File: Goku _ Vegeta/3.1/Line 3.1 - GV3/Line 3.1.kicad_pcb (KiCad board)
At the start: 2 copper layers, 112 parts, among them J1 Solenoid, J10 RIGHT HEADERS, J11 Kicker Voltmeter, J3 Motor 1, J4 Motor 3, J5 Motor 2, J6 Motor 4, J7 BATTERY POWER, J8 I2C TO MASTER, J9 LEFT HEADERS, Q2 BSC040N10NS5, U1 LM2587S-ADJ, U10 TPS62132, U11 TPS62133, U2 TB67H420FTG Dual/Single Motor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, U3 TB67H420FTG Dual/Single Motor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, U4 TB67H420FTG Dual/Single Motor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, U5 TB67H420FTG Dual/Single Motor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, U7 NXV55UNR, U9 DEV-16771

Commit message: move to 3.1
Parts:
- removed C1, C6: 100uF, Capacitor_THT:CP_Radial_D10.0mm_P5.00mm
- removed C10, C16: 0.1uF, Capacitor_SMD:C_0805_2012Metric
- removed C15, C8: 10uF, Capacitor_SMD:C_0805_2012Metric
- removed C17, C9: 3.3nF, Capacitor_SMD:C_0805_2012Metric
- removed C18, C7: 22uF, Capacitor_SMD:C_0805_2012Metric
- removed C2, C5: 1uF, Capacitor_SMD:C_0805_2012Metric
- removed C3, C4: 560uF, Capacitor_THT:CP_Radial_D18.0mm_P7.50mm
- removed D1: SS510, Diode_SMD:D_SOD-128
- removed D2, D3, D5: STTH2002G-TR, Package_TO_SOT_SMD:TO-263-2
- removed J1: Solenoid, TerminalBlock:TerminalBlock_bornier-2_P5.08mm
- removed J10: RIGHT HEADERS, Connector_PinHeader_2.54mm:PinHeader_1x24_P2.54mm_Vertical
- removed J3: Motor 1, Connector_PinSocket_2.54mm:PinSocket_1x06_P2.54mm_Vertical
- removed J5: Motor 2, Connector_PinSocket_2.54mm:PinSocket_1x06_P2.54mm_Vertical
- removed J6: Motor 4, Connector_PinSocket_2.54mm:PinSocket_1x06_P2.54mm_Vertical
- removed J7: BATTERY POWER, Connector_AMASS:AMASS_XT60-F_1x02_P7.20mm_Vertical
- removed J8: I2C TO MASTER, Connector_JST:JST_XH_B4B-XH-AM_1x04_P2.50mm_Vertical
- removed J9: LEFT HEADERS, Connector_PinHeader_2.54mm:PinHeader_1x24_P2.54mm_Vertical
- removed L1: 56uH, Inductor_SMD:L_Bourns_SRR1260
- removed L2, L3: 2.2uH, Inductor_SMD:L_Bourns_SRR1260
- removed Q2: BSC040N10NS5, Package_TO_SOT_SMD:TDSON-8-1
- removed R33, R35, R37, R39: 10K, Resistor_SMD:R_0805_2012Metric
- removed R34, R36, R38: 12R, Resistor_SMD:R_0805_2012Metric
- removed U1: LM2587S-ADJ, LM2587S-ADJ:VREG_TPS79625KTTR
- removed U10: TPS62132, Package_DFN_QFN:VQFN-16-1EP_3x3mm_P0.5mm_EP1.68x1.68mm_ThermalVias
- removed U11: TPS62133, Package_DFN_QFN:VQFN-16-1EP_3x3mm_P0.5mm_EP1.68x1.68mm_ThermalVias
- removed U2, U3, U4, U5: TB67H420FTG Dual/Single Motor Driver Carrier, TB67H420FTG Dual_Single Motor Driver Carrier:TB67H420FTG DualSingle Motor Driver Carrier
- removed U7: NXV55UNR, NXV55UNR:TRANS_BC846B,215
- removed U9: DEV-16771, DEV-16771:MODULE_DEV-16771
- added J12: RIGHT HEADERS, Connector_PinHeader_2.54mm:PinHeader_1x24_P2.54mm_Vertical, F.Cu at (139.0, 247.2)
- added J13: MID HEADERS, Connector_PinHeader_2.54mm:PinHeader_1x05_P2.54mm_Vertical, F.Cu at (144.9, 183.5)
- added J2: BACKUP 5V, Connector_AMASS:AMASS_XT30U-F_1x02_P5.0mm_Vertical, F.Cu at (78.8, 124.5)
- added U8: DEV-16771, DEV-16771:MODULE_DEV-16771, F.Cu at (150.0, 218.0)
- A1, A10, A11, A12, A13, A14, A15, A16, A2, A3, A4, A5, A6, A7, A8, A9, LED1, LED10, LED11, LED12, LED13, LED14, LED15, LED16, LED2, LED3, LED4, LED5, LED6, LED7, LED8, LED9, R10, R12, R14, R16, R26, R28: moved to B.Cu
- J11: value Kicker Voltmeter -> LEFT HEADERS; footprint TerminalBlock:TerminalBlock_bornier-2_P5.08mm -> Connector_PinHeader_2.54mm:PinHeader_1x24_P2.54mm_Vertical
- J4: value Motor 3 -> I2C; footprint Connector_PinSocket_2.54mm:PinSocket_1x06_P2.54mm_Vertical -> Connector_AMASS:AMASS_XT30U-F_1x02_P5.0mm_Vertical
- R1: value 2K94 -> 36R; moved to B.Cu
- R11, R13, R15, R25, R27, R31, R9: value 12R -> 10K; moved to B.Cu
- R17, R19, R21, R23, R4, R6: value 12R -> 36R; moved to B.Cu
- R18, R20, R22, R24, R5, R7, R8: value 10K -> 36R; moved to B.Cu
- R2: value 57K -> 36R; moved to B.Cu
- R29: value CT6EP103 -> 10K; footprint POT_CT-6EP_NDC:POT_CT-6EP_NDC -> Resistor_SMD:R_0805_2012Metric; moved to B.Cu
- R3: value 1K5 -> 36R; moved to B.Cu
- R30, R32: value 100K -> 10K; moved to B.Cu
- moved A2 149.1 mm to (230.0, 150.0), turned to 90 degrees
- moved R11 124.0 mm to (154.0, 227.0), turned to -90 degrees
- moved R3 123.2 mm to (146.0, 227.0), turned to 90 degrees
- moved R2 119.4 mm to (227.0, 154.0), turned to 180 degrees
- moved A6 118.9 mm to (200.0, 150.0), turned to 90 degrees
- moved R10 112.1 mm to (227.0, 146.0)
- moved A3 109.8 mm to (150.0, 230.0)
- moved LED2 109.7 mm to (227.0, 150.0), turned to -90 degrees
- moved A1 98.1 mm to (150.0, 70.0), turned to 180 degrees
- moved LED3 97.7 mm to (150.0, 227.0), turned to 180 degrees
- moved J11 95.2 mm to (161.0, 247.2), turned to 180 degrees
- moved A7 88.3 mm to (150.0, 200.0)
- moved R6 87.2 mm to (197.0, 154.0), turned to 180 degrees
- moved A5 84.7 mm to (150.0, 100.0), turned to 180 degrees
- moved A11 84.5 mm to (170.0, 150.0), turned to 90 degrees
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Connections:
- A1 pad 1: +3V3 -> +5V
- A1 pad 2: /SEN1 -> /21
- A10 pad 1: +3V3 -> +5V
- A10 pad 2: /SEN1 -> /38
- A11 pad 1: +3V3 -> +5V
- A11 pad 2: /SEN1 -> /39
- A12 pad 1: +3V3 -> +5V
- A12 pad 2: /SEN1 -> /40
- A13 pad 1: +3V3 -> +5V
- A13 pad 2: /SEN1 -> /41
- A14 pad 1: +3V3 -> +5V
- A14 pad 2: /SEN1 -> /14
- A15 pad 1: +3V3 -> +5V
- A15 pad 2: /SEN1 -> /15
- A16 pad 1: +3V3 -> +5V
- A16 pad 2: /SEN1 -> /16
- A2 pad 1: +3V3 -> +5V
- A2 pad 2: /SEN1 -> /26
- A3 pad 1: +3V3 -> +5V
- A3 pad 2: /SEN1 -> /24
- A4 pad 1: +3V3 -> +5V
- A4 pad 2: /SEN1 -> /23
- A5 pad 1: +3V3 -> +5V
- A5 pad 2: /SEN1 -> /20
- A6 pad 1: +3V3 -> +5V
- A6 pad 2: /SEN1 -> /27
- A7 pad 1: +3V3 -> +5V
- A7 pad 2: /SEN1 -> /25
- A8 pad 1: +3V3 -> +5V
- A8 pad 2: /SEN1 -> /22
- A9 pad 1: +3V3 -> +5V
- A9 pad 2: /SEN1 -> /17
- J11 pad 1: Net-(D1-K) -> GND
- J11 pad 2: GND -> /0
- J4 pad 1: Net-(J4-Pin_1) -> /19
- J4 pad 2: Net-(J4-Pin_2) -> /18
- LED1 pad 1: /MSFTDRN -> GND
- LED10 pad 1: /MSFTDRN -> GND
- LED11 pad 1: /MSFTDRN -> GND
- LED12 pad 1: /MSFTDRN -> GND
- LED13 pad 1: /MSFTDRN -> GND
- LED14 pad 1: /MSFTDRN -> GND
- LED15 pad 1: /MSFTDRN -> GND
- LED16 pad 1: /MSFTDRN -> GND
- LED2 pad 1: /MSFTDRN -> GND
- LED3 pad 1: /MSFTDRN -> GND
- LED4 pad 1: /MSFTDRN -> GND
- LED5 pad 1: /MSFTDRN -> GND
- LED6 pad 1: /MSFTDRN -> GND
- LED7 pad 1: /MSFTDRN -> GND
- LED8 pad 1: /MSFTDRN -> GND
- LED9 pad 1: /MSFTDRN -> GND
- R1 pad 1: Net-(U1-COMP) -> +5V
- R1 pad 2: Net-(C2-Pad1) -> Net-(LED1-Pad2)
- R10 pad 2: /SEN1 -> /26
- R11 pad 1: +3V3 -> GND
- R11 pad 2: Net-(LED4-Pad2) -> /24
- R12 pad 2: /SEN1 -> /23
- R13 pad 1: +3V3 -> GND
- R13 pad 2: Net-(LED5-Pad2) -> /20
- R14 pad 2: /SEN1 -> /27
- R15 pad 1: +3V3 -> GND
- R15 pad 2: Net-(LED6-Pad2) -> /25
- R16 pad 2: /SEN1 -> /22
- R17 pad 1: +3V3 -> +5V
- R17 pad 2: Net-(LED7-Pad2) -> Net-(LED9-Pad2)
- R18 pad 1: GND -> +5V
- R18 pad 2: /SEN1 -> Net-(LED10-Pad2)
- R19 pad 1: +3V3 -> +5V
- R19 pad 2: Net-(LED8-Pad2) -> Net-(LED11-Pad2)
- R2 pad 1: Net-(D1-K) -> +5V
- R2 pad 2: Net-(R2-Pad2) -> Net-(LED2-Pad2)
- R20 pad 1: GND -> +5V
- R20 pad 2: /SEN1 -> Net-(LED12-Pad2)
- R21 pad 1: +3V3 -> +5V
- R21 pad 2: Net-(LED9-Pad2) -> Net-(LED13-Pad2)
- R22 pad 1: GND -> +5V
- R22 pad 2: /SEN1 -> Net-(LED14-Pad2)
- R23 pad 1: +3V3 -> +5V
- R23 pad 2: Net-(LED10-Pad2) -> Net-(LED15-Pad2)
- R24 pad 1: GND -> +5V
- R24 pad 2: /SEN1 -> Net-(LED16-Pad2)
- R25 pad 1: +3V3 -> GND
- R25 pad 2: Net-(LED11-Pad2) -> /17
- R26 pad 2: /SEN1 -> /38
- R27 pad 1: +3V3 -> GND
- R27 pad 2: Net-(LED12-Pad2) -> /39
- R28 pad 2: /SEN1 -> /40
- R29 pad 1: Net-(U1-FB) -> GND
- R29 pad 2: Net-(U1-FB) -> /41
- R3 pad 1: Net-(U1-FB) -> +5V
- R3 pad 2: GND -> Net-(LED3-Pad2)
- R30 pad 1: Net-(U10-PG) -> GND
- R30 pad 2: +3V3 -> /14
- R31 pad 1: +3V3 -> GND
- R31 pad 2: Net-(LED13-Pad2) -> /15
- R32 pad 1: Net-(U11-PG) -> GND
- R32 pad 2: +5V -> /16
- R4 pad 1: +3V3 -> +5V
- R4 pad 2: Net-(LED1-Pad2) -> Net-(LED4-Pad2)
- R5 pad 1: GND -> +5V
- R5 pad 2: /SEN1 -> Net-(LED5-Pad2)
- R6 pad 1: +3V3 -> +5V
- R6 pad 2: Net-(LED2-Pad2) -> Net-(LED6-Pad2)
- R7 pad 1: GND -> +5V
- R7 pad 2: /2 -> Net-(LED7-Pad2)
- R8 pad 1: GND -> +5V
- R8 pad 2: /SEN1 -> Net-(LED8-Pad2)
- R9 pad 1: +3V3 -> GND
- R9 pad 2: Net-(LED3-Pad2) -> /21
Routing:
- net +5V: track 0.00 -> 664.1 mm, vias 0 -> 13
- net /21: track 0.00 -> 186.8 mm
- net /20: track 0.00 -> 152.0 mm
- net /23: track 0.00 -> 121.8 mm
- net /17: track 0.00 -> 118.8 mm
- net /26: track 0.00 -> 110.6 mm
- net /22: track 0.00 -> 107.1 mm
- net /19: track 0.00 -> 99.7 mm, vias 0 -> 1
- net /16: track 0.00 -> 98.2 mm
- net /38: track 0.00 -> 97.8 mm
- net /18: track 0.00 -> 92.8 mm, vias 0 -> 1
- net /39: track 0.00 -> 83.0 mm
- net /27: track 0.00 -> 81.2 mm, vias 0 -> 2
- net /15: track 0.00 -> 80.5 mm
- net /14: track 0.00 -> 68.7 mm
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- added copper zone on B.Cu, net GND
- added copper zone on F.Cu, net GND
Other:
- board outline added: 206 x 197.4 mm
- board text added: "Designed by Hugh Phan - September 2023"
- board text added: "Fort Street's Team Silverback Hugh Phan Jayden Nguyen Issey Lee Jack Sumner KZ KC"
- board text added: "MOTOR A"
- board text added: "MOTOR B"
- board text added: "MOTOR C"
- board text added: "MOTOR D"
- board text added: "TEENSY 4.1 3V3 LINES NOT CONNECTED"

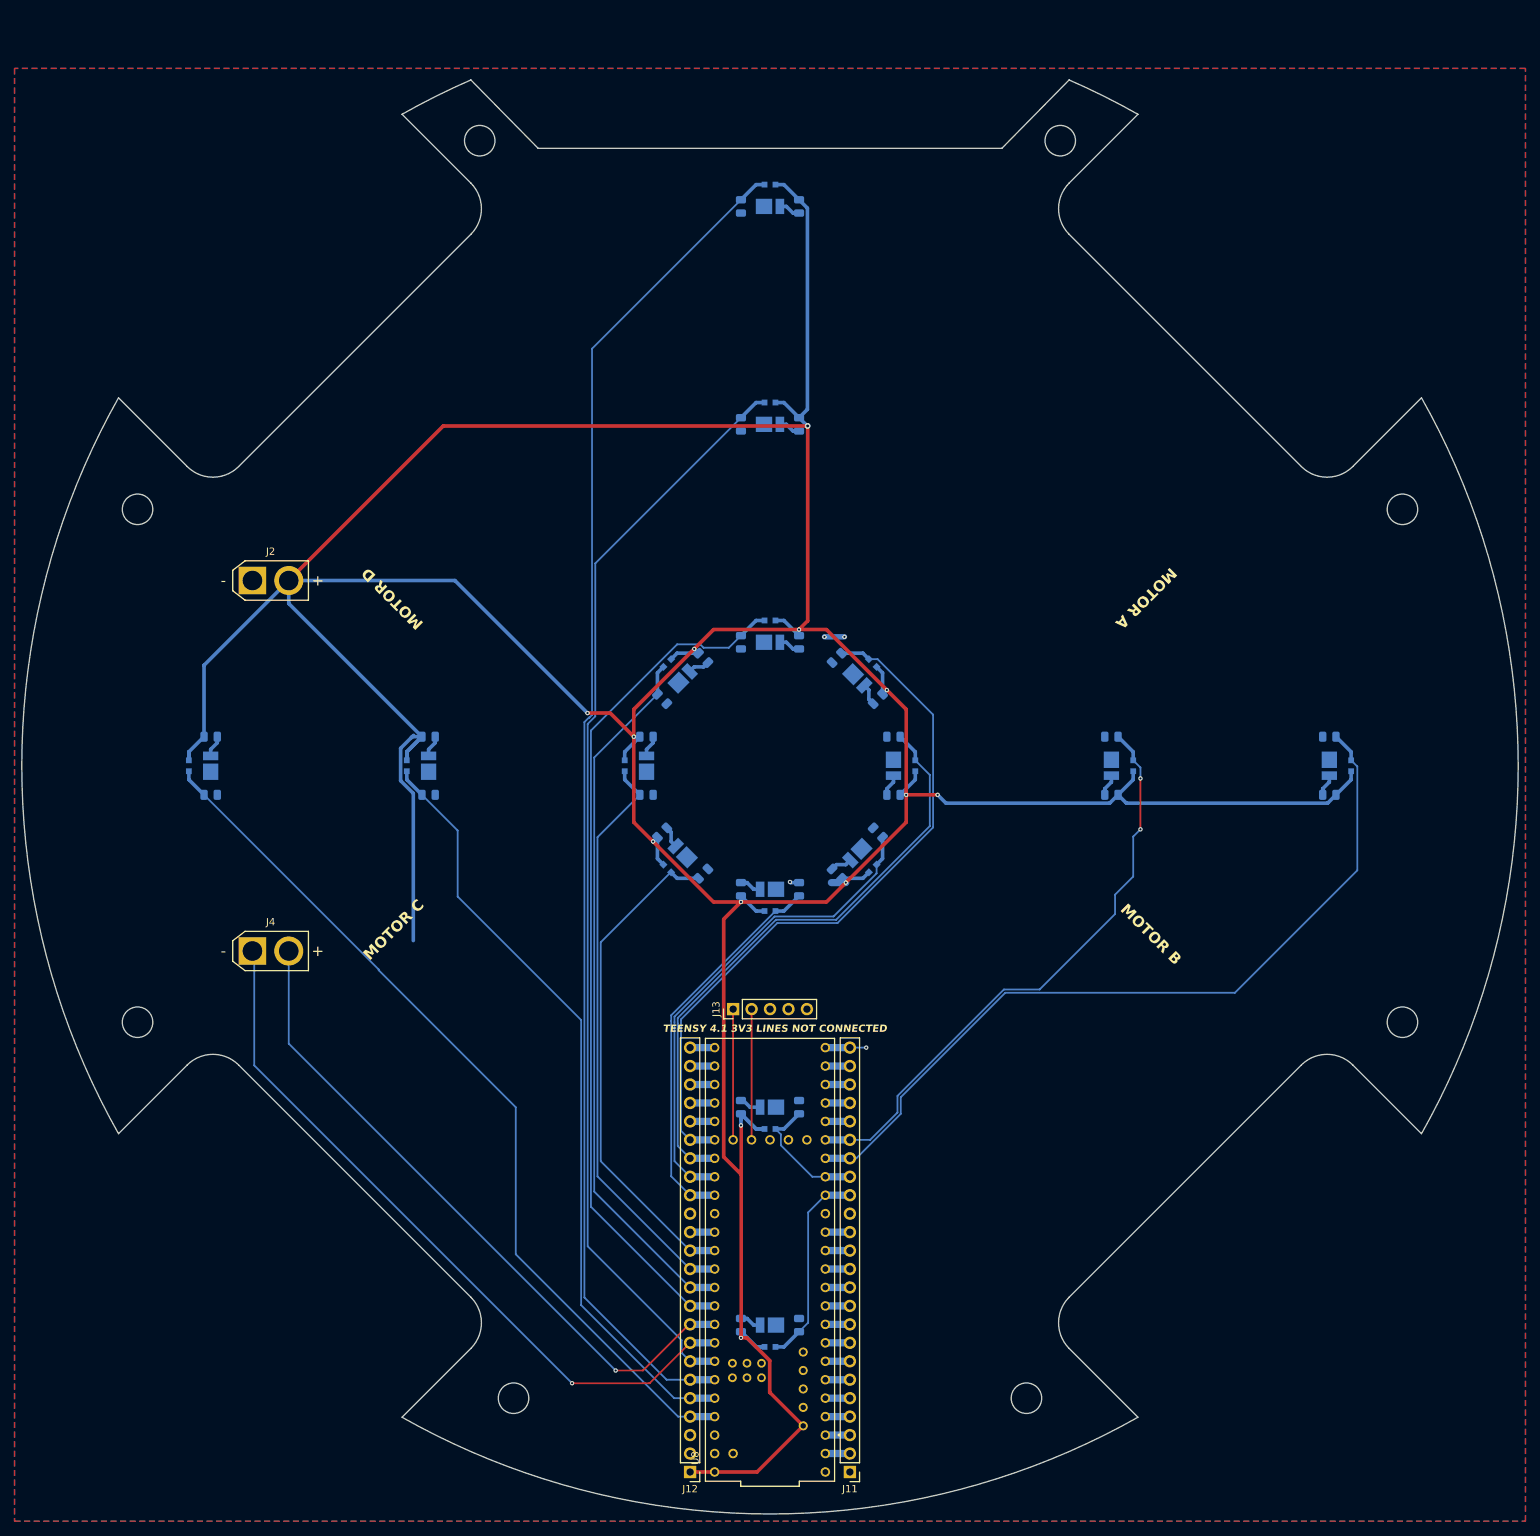
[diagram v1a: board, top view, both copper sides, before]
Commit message: MAIN 3.1 DONE no silkscreen
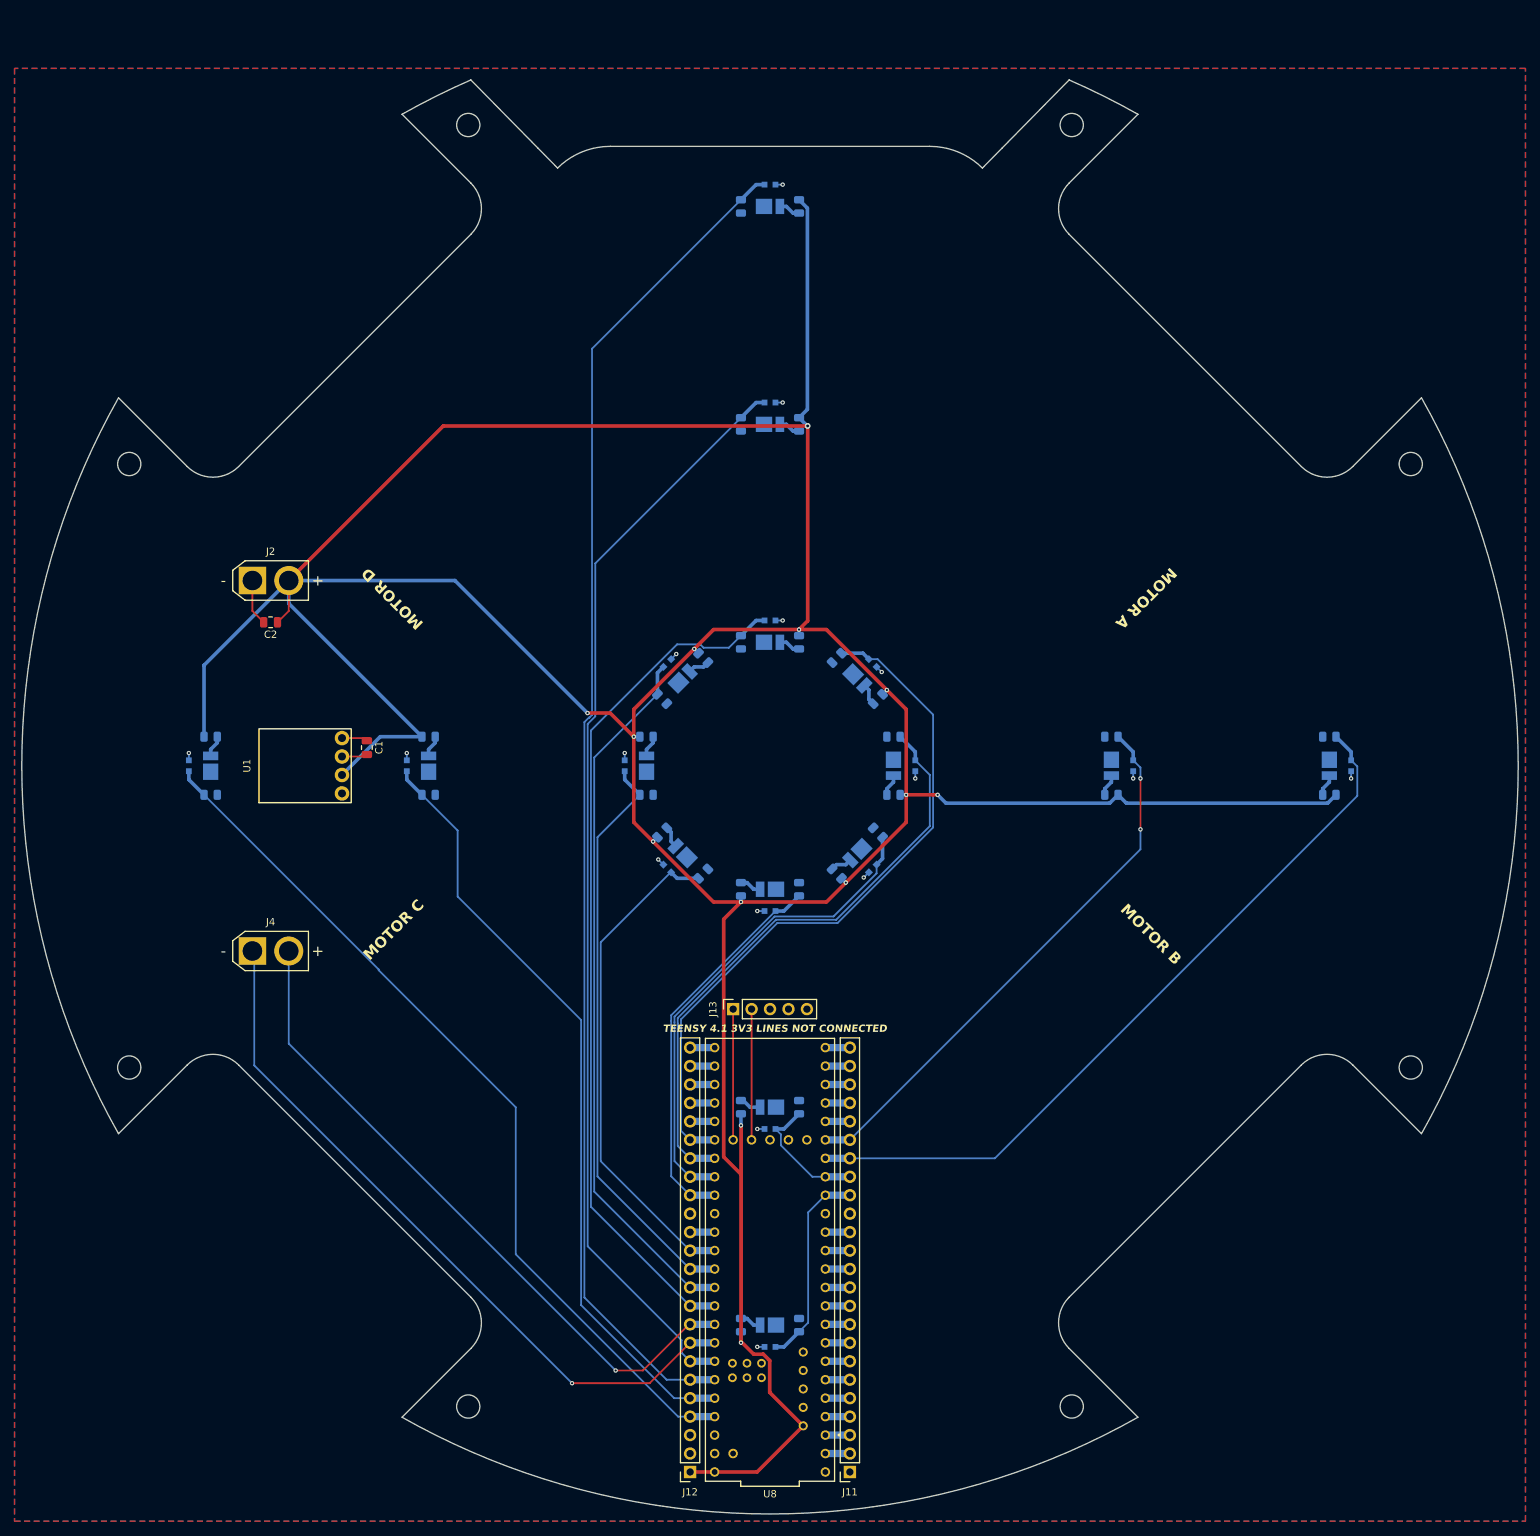
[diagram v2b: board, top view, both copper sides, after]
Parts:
- added C1: 10uF, Capacitor_SMD:C_0805_2012Metric, F.Cu at (94.5, 147.5)
- added C2: 10uF, Capacitor_SMD:C_0805_2012Metric, F.Cu at (81.2, 130.2)
- added U1: ~, Converter_DCDC:Pololu 3.3V, 500mA Step-Down Voltage Regulator D24V5F3, F.Cu at (86.0, 150.0)
- J11, J12: footprint Connector_PinHeader_2.54mm:PinHeader_1x24_P2.54mm_Vertical -> Connector_PinSocket_2.54mm:PinSocket_1x24_P2.54mm_Vertical
- J13: footprint Connector_PinHeader_2.54mm:PinHeader_1x05_P2.54mm_Vertical -> Connector_PinSocket_2.54mm:PinSocket_1x05_P2.54mm_Vertical
- J2: value BACKUP 5V -> 5V LINE
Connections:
- A1 pad 1: +5V -> +3V3
- A10 pad 1: +5V -> +3V3
- A11 pad 1: +5V -> +3V3
- A12 pad 1: +5V -> +3V3
- A13 pad 1: +5V -> +3V3
- A14 pad 1: +5V -> +3V3
- A15 pad 1: +5V -> +3V3
- A16 pad 1: +5V -> +3V3
- A2 pad 1: +5V -> +3V3
- A3 pad 1: +5V -> +3V3
- A4 pad 1: +5V -> +3V3
- A5 pad 1: +5V -> +3V3
- A6 pad 1: +5V -> +3V3
- A7 pad 1: +5V -> +3V3
- A8 pad 1: +5V -> +3V3
- A9 pad 1: +5V -> +3V3
- J12 pad 1: unconnected-(J12-Pin_1-Pad1) -> +5V
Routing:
- net +5V: track 664.1 -> 571.1 mm
- net +3V3: track 0.00 -> 19.6 mm, vias 0 -> 16
- net GND: track 2.37 -> 11.0 mm, vias 1 -> 0
- net /26: track 110.6 -> 103.3 mm
- net /27: track 81.2 -> 76.7 mm
- net (no net): track 2.75 -> 0.00 mm, vias 2 -> 0
- net /32: track 5.63 -> 3.38 mm, vias 1 -> 0
- net /6: track 4.07 -> 3.38 mm
- added copper zone on F.Cu, net +3V3
- removed copper zone on F.Cu, net GND
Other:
- outline, holes or cut-outs redrawn

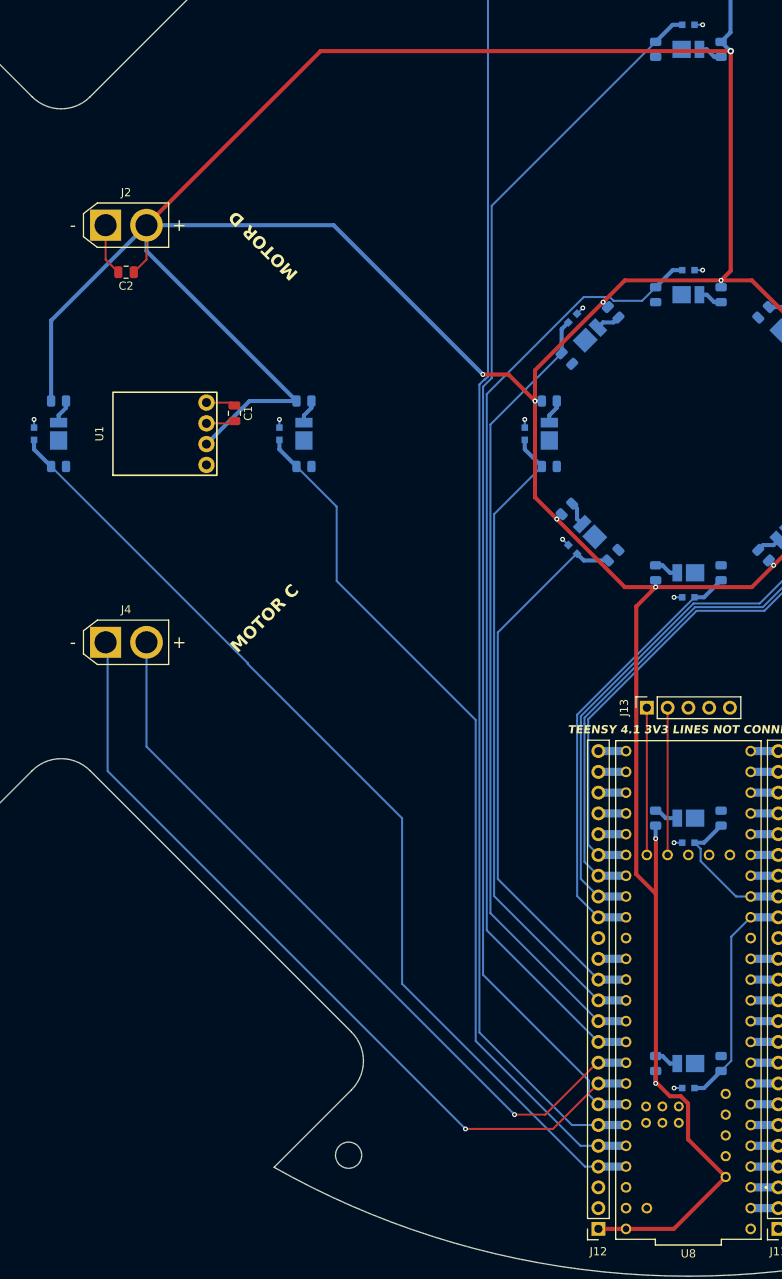
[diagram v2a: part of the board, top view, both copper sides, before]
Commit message: Main and Line 3.1 done w/ silkscreen
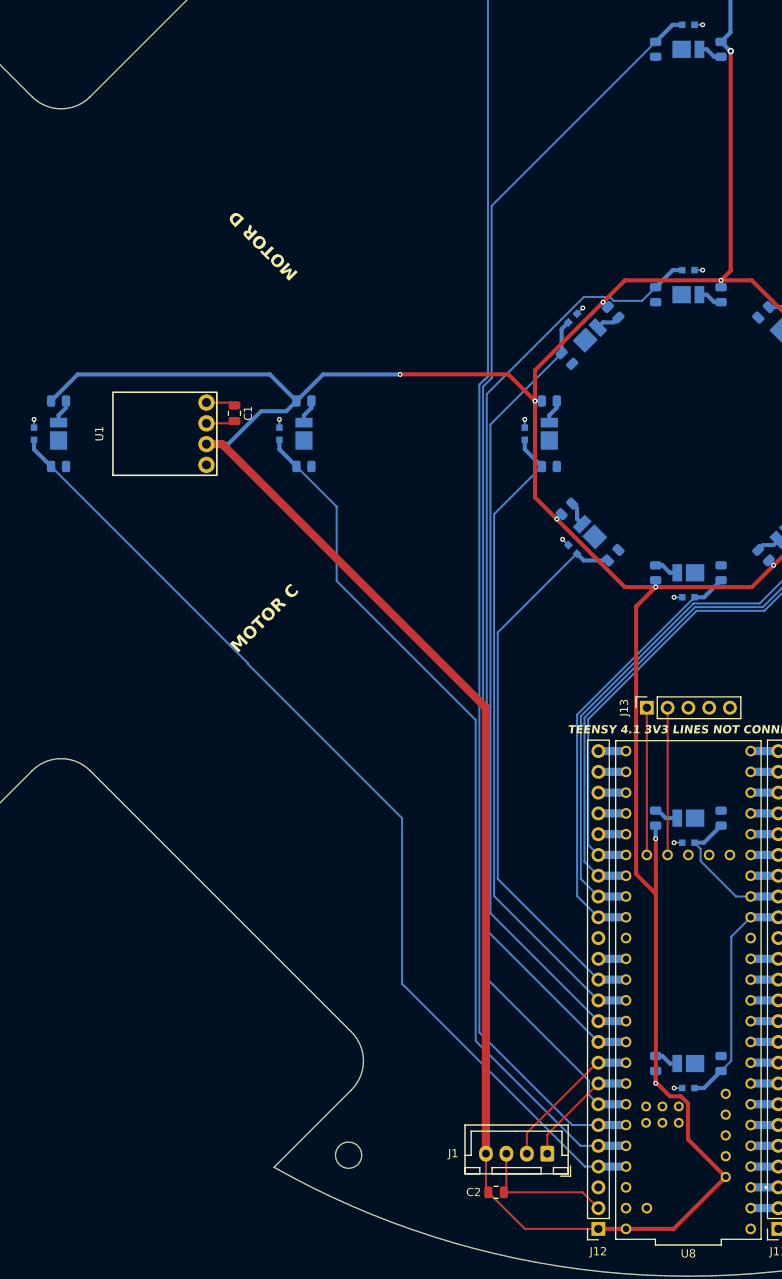
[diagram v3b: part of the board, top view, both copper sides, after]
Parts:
- removed J2: 5V LINE, Connector_AMASS:AMASS_XT30U-F_1x02_P5.0mm_Vertical
- removed J4: I2C, Connector_AMASS:AMASS_XT30U-F_1x02_P5.0mm_Vertical
- added G***: LOGO, LOGO, B.Cu at (242.8, 170.2)
- added G***: LOGO, LOGO, B.Cu at (196.3, 197.8)
- added G***: LOGO, LOGO, B.Cu at (242.3, 132.2)
- added G***: LOGO, LOGO, B.Cu at (193.5, 105.8)
- added G***: LOGO, LOGO, B.Cu at (103.4, 196.2)
- added G***: LOGO, LOGO, B.Cu at (102.3, 103.1)
- added G***: LOGO, LOGO, B.Cu at (57.0, 161.0)
- added G***: LOGO, LOGO, B.Cu at (57.0, 128.0)
- added J1: Line, Connector_JST:JST_XH_B4B-XH-A_1x04_P2.50mm_Vertical, F.Cu at (132.8, 238.0)
- moved C2 121.3 mm to (126.5, 242.8), turned to 0 degrees
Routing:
- net /19: track 99.7 -> 14.6 mm, vias 1 -> 0
- net /18: track 92.8 -> 18.4 mm, vias 1 -> 0
- net +5V: track 571.1 -> 559.4 mm
- net GND: track 11.0 -> 21.8 mm
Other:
- board text added: "Fort Street's Team Silverback"
- board text added: "Hugh Phan"
- board text added: "Issey Lee"
- board text added: "Jack Sumner"
- board text added: "Jayden Nguyen"
- board text added: "V3"

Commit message: main 3.1 fixup
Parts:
- moved G*** 14.2 mm to (42.8, 128.0)
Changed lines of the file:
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@@
   )
   (footprint "LOGO" (layer "B.Cu")
-    (at 57 128 90)
+    (at 42.75 128 90)
     (attr board_only exclude_from_pos_files exclude_from_bom)
     (fp_text reference "G***" (at 0 0 90) (layer "B.SilkS") hide
